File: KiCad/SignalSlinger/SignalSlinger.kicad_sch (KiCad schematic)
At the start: 56 parts, among them J101 Conn_01x02, J102 Conn_01x03, J103 Conn_01x02, J104 Conn_01x02, J105 Conn_01x04, J106 Conn_01x02, J107 DB9 Female, P101 ISP/PDI, Q101 BSS84W-7-F, Q102 BSS138W-7-F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

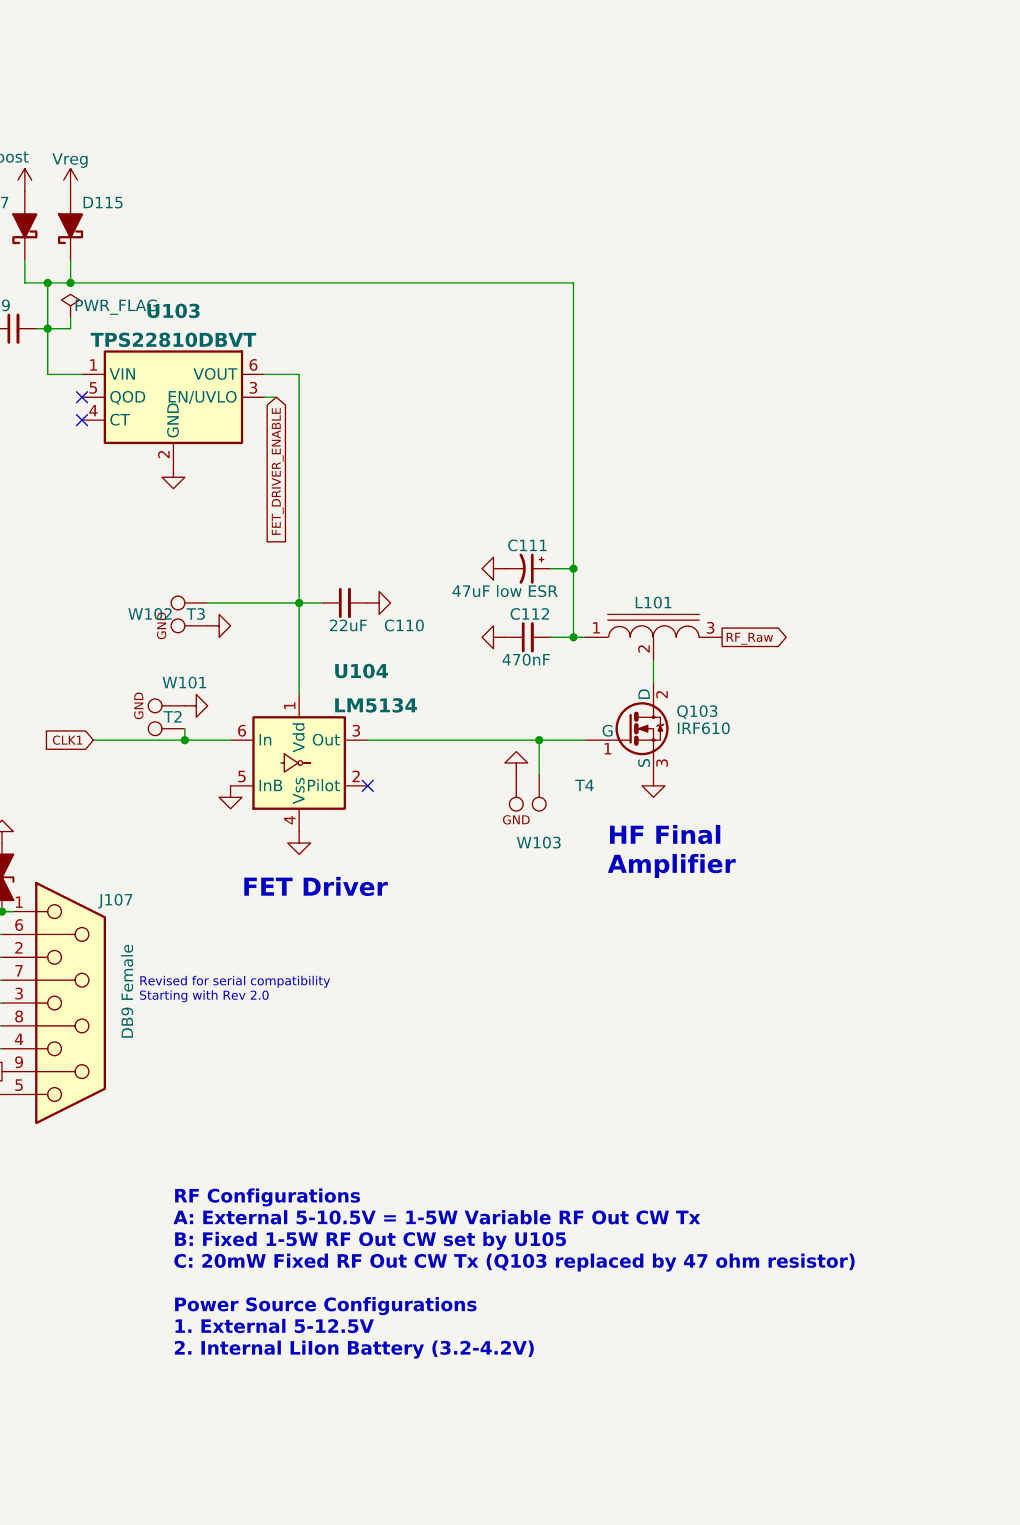
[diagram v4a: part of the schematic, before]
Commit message: Comment updates
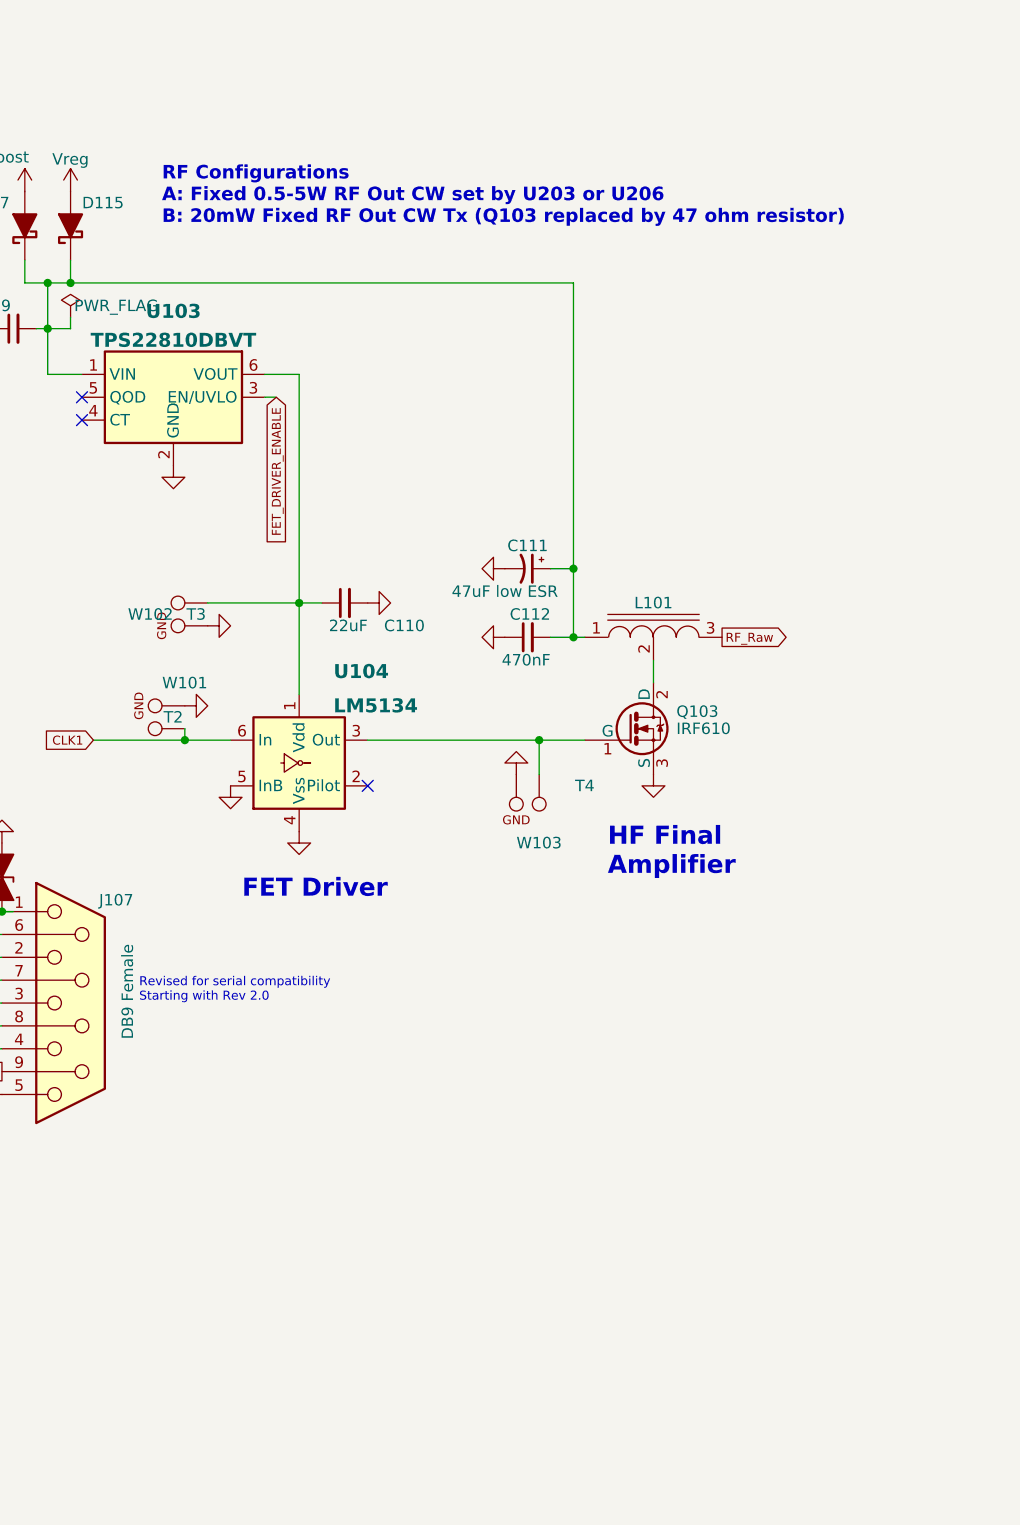
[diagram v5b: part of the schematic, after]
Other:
- note added: "RF Configurations A: Fixed 0.5-5W RF Out CW set by U203 or U206 B: 20mW Fixed RF Out CW Tx (Q103 replaced by 47 ohm resistor)"
- note removed: "RF Configurations A: External 5-10.5V = 1-5W Variable RF Out CW Tx B: Fixed 1-5W RF Out CW set by U105 C: 20mW Fixed RF Out CW Tx (Q103 replaced by 47 ohm resistor) Power Source Configurations 1. External 5-12.5V 2. Internal LiIon Battery (3.2-4.2V)"
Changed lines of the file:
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@@
     (effects (font (size 1.27 1.27)) (justify left bottom))
+  )
+  (text "RF Configurations\nA: Fixed 0.5-5W RF Out CW set by U203 or U206\nB: 20mW Fixed RF Out CW Tx (Q103 replaced by 47 ohm resistor)"
+    (at 207.01 38.1 0)
+    (effects (font (size 1.5 1.5) (thickness 0.3) bold) (justify left bottom))
   )
   (text "HF Final\nAmplifier" (at 256.54 110.49 0)
     (effects (font (size 2.0066 2.0066) (thickness 0.4013) bold) (justify left bottom))
   )
-  (text "RF Configurations\nA: External 5-10.5V = 1-5W Variable RF Out CW Tx\nB: Fixed 1-5W RF Out CW set by U105\nC: 20mW Fixed RF Out CW Tx (Q103 replaced by 47 ohm resistor)\n\nPower Source Configurations\n1. External 5-12.5V\n2. Internal LiIon Battery (3.2-4.2V)\n\n"
-    (at 208.28 166.37 0)
-    (effects (font (size 1.5 1.5) (thickness 0.3) bold) (justify left bottom))
-  )
   (text "On/Off" (at 46.99 152.4 0)

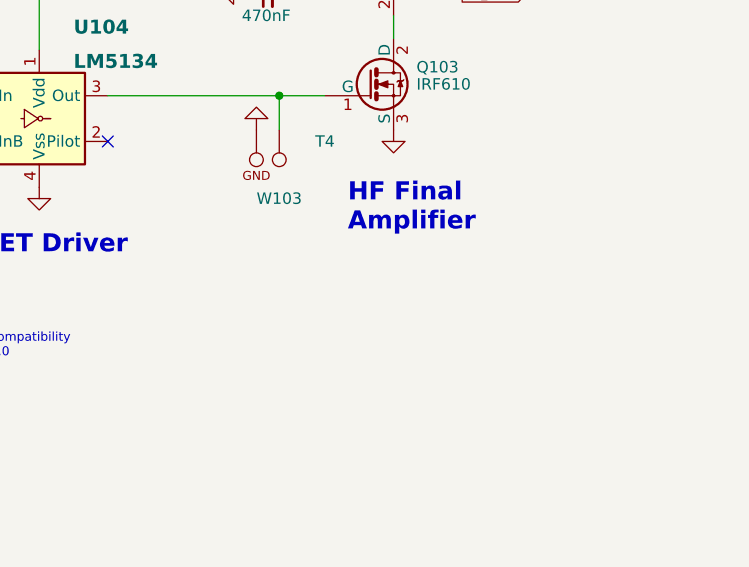
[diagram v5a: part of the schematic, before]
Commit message: Added L101 Construction
Schemtic change
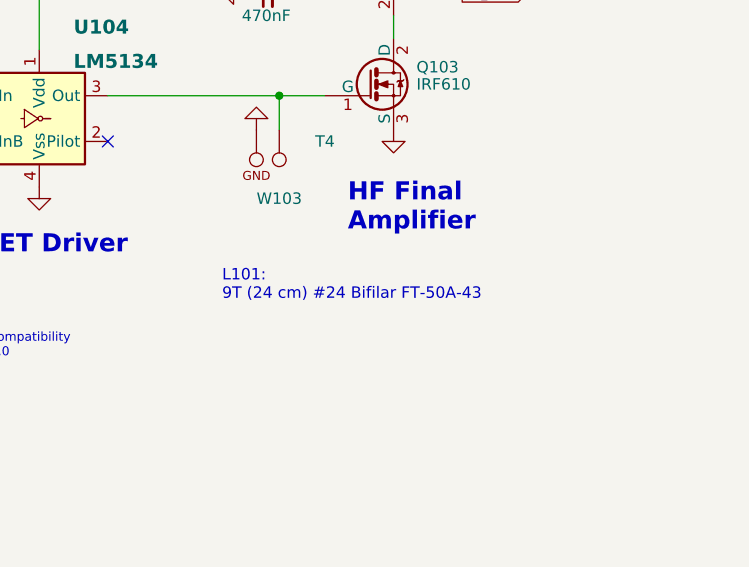
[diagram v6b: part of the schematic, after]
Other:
- note added: "L101: 9T (24 cm) #24 Bifilar FT-50A-43"
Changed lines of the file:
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@@
     (effects (font (size 2.0066 2.0066) (thickness 0.4013) bold) (justify left bottom))
+  )
+  (text "L101:\n9T (24 cm) #24 Bifilar FT-50A-43" (at 242.57 118.11 0)
+    (effects (font (size 1.27 1.27)) (justify left bottom))
   )
   (text "RED" (at 114.3 162.56 0)

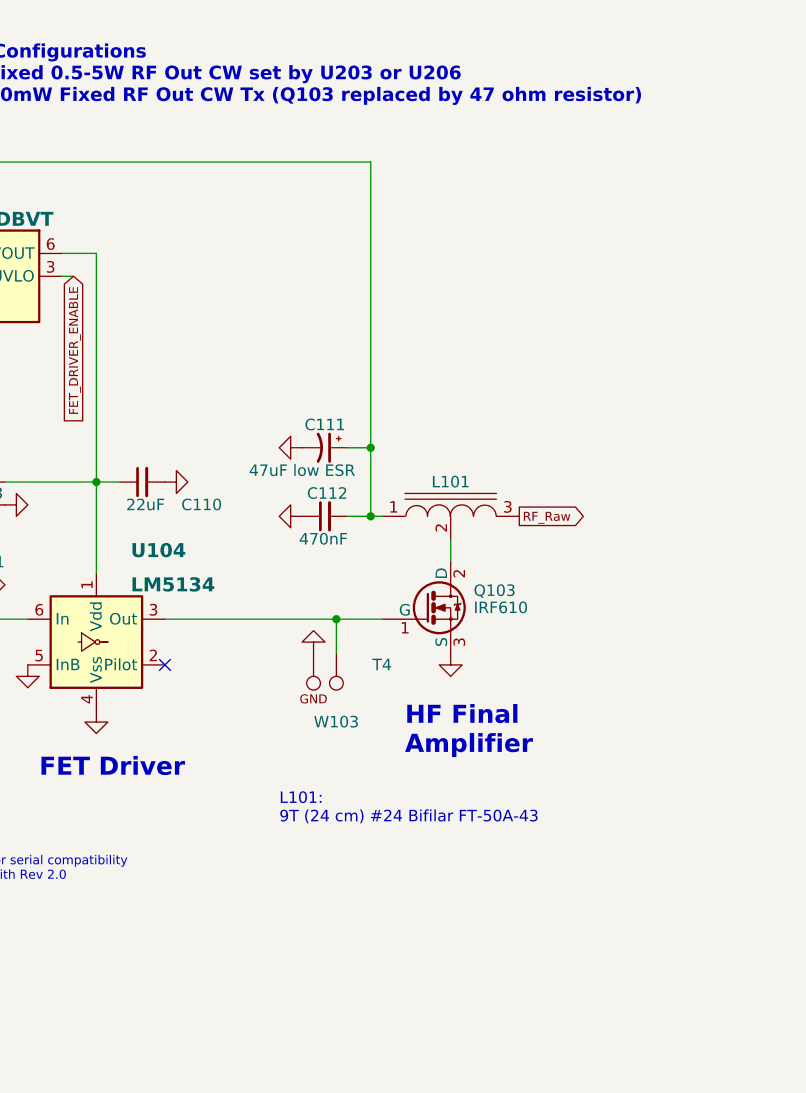
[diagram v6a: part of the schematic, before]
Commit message: Extensive Cleanup
BOM scrub
Added jumpers for foxoring power level
PCB ground plane improvements
Updated Gerbers
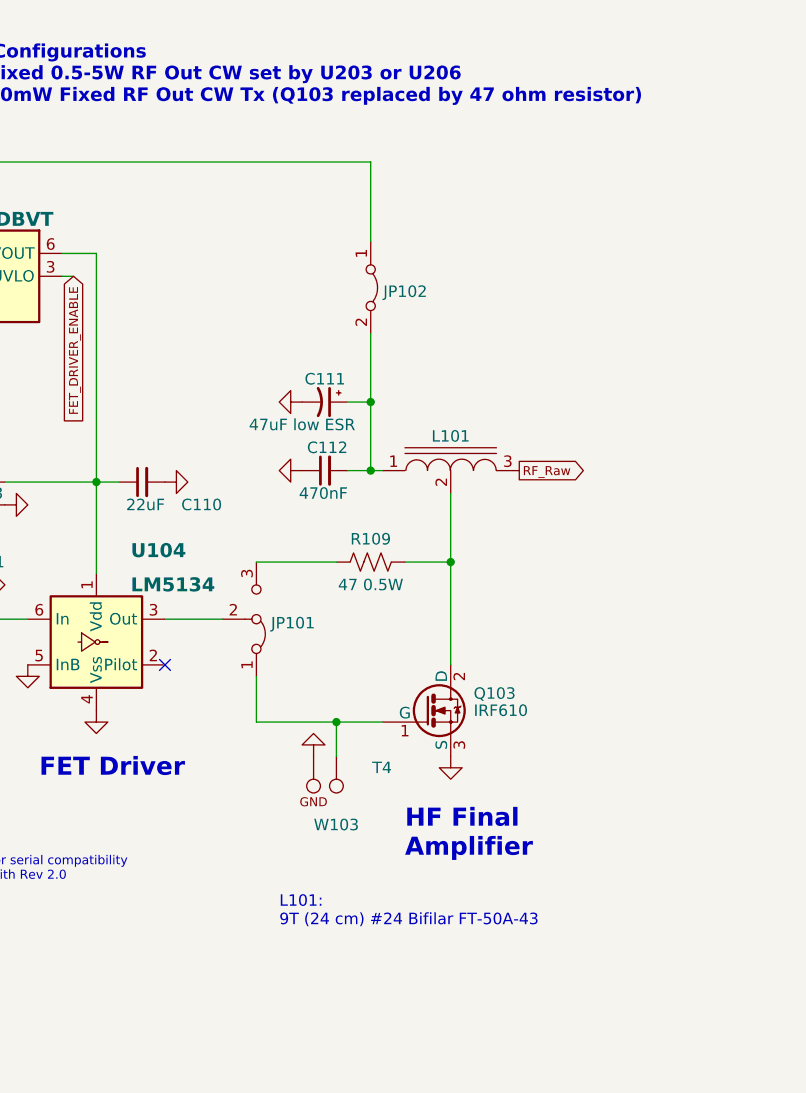
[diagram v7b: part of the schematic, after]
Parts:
- added JP101: NetTie_Jumper_3_Bridged12, Jumper:Jumper_THT_1x03_Bridged12_P1.27mm_Vertical, symbol Jumper:NetTie_Jumper_3_Bridged12
- added JP102: NetTie_Jumper_2_Bridged, Jumper:Jumper_THT_1x02_P1.27mm_Vertical, symbol Jumper:NetTie_Jumper_2_Bridged
- added R109: 47 0.5W, Resistor_THT:R_Axial_DIN0204_L3.6mm_D1.6mm_P2.54mm_Vertical, symbol Device:R_Small_US
- R107, R108: footprint Capacitor_SMD:C_0805_2012Metric -> Resistor_SMD:R_0805_2012Metric
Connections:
- net at C109.2, D107.1 (K), D115.1 (K)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: now also JP102.1 (A); no longer C111.1, C112.2, L101.1
- net at Q103.1 (G), W103.1: now also JP101.1 (A); no longer U104.3 (Out)
- net at L101.2 (TAP), Q103.2 (D): now also R109.1
- new net: C111.1, C112.2, JP102.2 (B), L101.1
- new net: JP101.2 (C), U104.3 (Out)
- new net: JP101.3 (B), R109.2
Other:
- moved on the sheet: C111, C112, L101, Q103, W103
